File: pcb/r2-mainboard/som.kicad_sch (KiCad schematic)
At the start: 14 parts, among them J21 MICRO_SD(TFC-WPAPR-08), J26 BTH-060-01-L-D-A-K-TR, J27 BTH-060-01-L-D-A-K-TR, X2 PCM-071

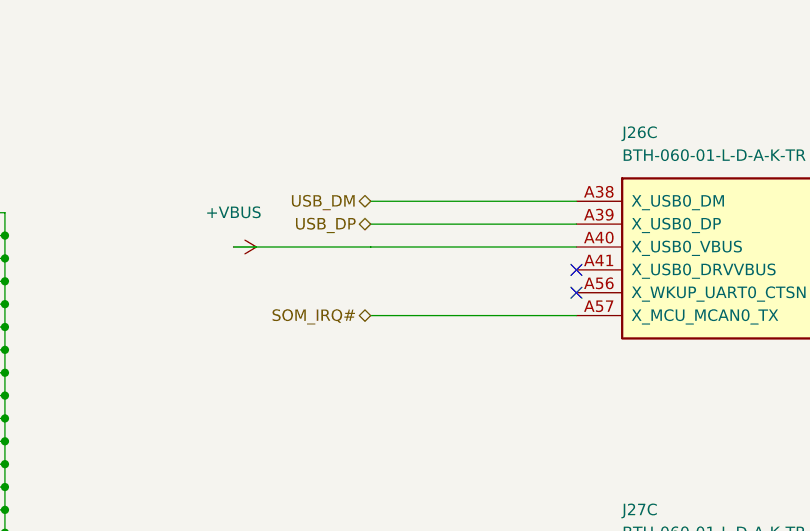
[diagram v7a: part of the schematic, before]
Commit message: R2: place the two receptacles from X2, and fix three bugs found doing it
The connectors move as one now. tools/place_som.py reads X2's position and
rotation, snaps J26/J27 onto their exact offsets, and puts all three into a
KiCad group -- so from here you drag the SoM, not three parts that have to
agree with each other. It backs up the board, refuses to run while KiCad is
open, and re-runs the geometry check to prove its own result.

That symmetry is the reason this is a tool and not an instruction: the two
offsets are exact negatives about X2's origin, so an error of the wrong kind
does not shift a connector slightly, it puts J26 where J27 belongs. The
module still seats and every one of 240 nets is on the wrong receptacle.

Three bugs, all mine:

1. check_pcb_connectors.py had the rotation sign backwards, which SWAPPED
   the two expected positions. It reported a hand placement that was 0.9 mm
   and 0.2 mm out as 22 mm out, and would equally have blessed a board with
   the connectors exchanged. Settled empirically from a drill export rather
   than by reasoning: J26's alignment holes are asymmetric in x, so they
   distinguish the conventions. Confirmed twice, against X2's M2.5 holes too.

2. gen_som_footprint.py wrote (layer "User.Drawings"), which is KiCad's
   display alias; a board file needs the canonical Dwgs.User. The footprint
   editor accepts the alias, so the library exported fine -- but on import
   Pcbnew put those rects on a layer literally named "Rescue", and from then
   on kicad-cli could not read the board at all. Every pcb subcommand had
   been failing since the board was created.

3. Which made a third bug visible: check_pcb.py read /tmp/r2-drc.json
   without checking that the run succeeded, so it reported the previous
   run's numbers. A board that would not open was described as having 4250
   DRC violations. It now deletes the report first and says DID NOT RUN.

Real DRC, now that it runs: 742 violations, 499 unconnected -- which is what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
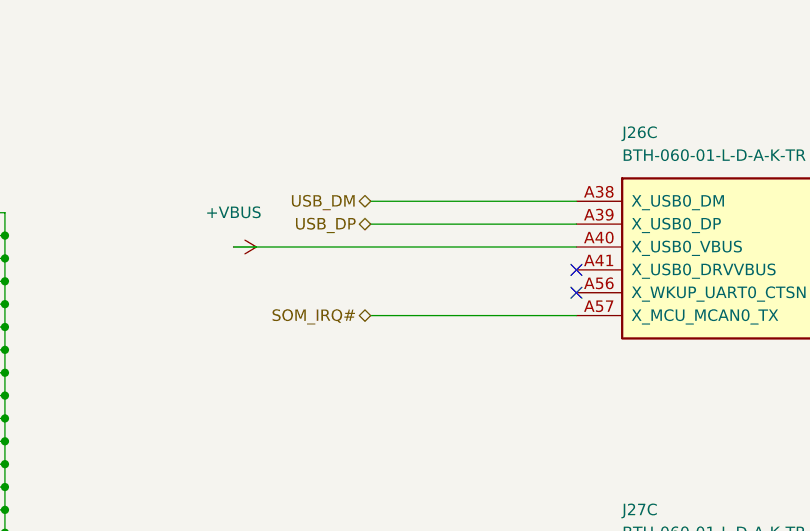
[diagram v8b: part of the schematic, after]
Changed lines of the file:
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@@
 	(wire
 		(pts
-			(xy 154.94 43.18) (xy 139.7 43.18)
+			(xy 139.7 43.18) (xy 177.8 43.18)
 		)
 		(stroke
@@
 		)
 		(stroke
-			(width 0)
-			(type default)
-		)
-	)
-	(wire
-		(pts
-			(xy 177.8 43.18) (xy 154.94 43.18)
-		)
-		(stroke
